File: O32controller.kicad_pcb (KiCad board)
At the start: 4 copper layers, 27 x 27 mm, 15 parts, among them J1 Conn_01x08_MountingPin, J2 Conn_01x02, J3 Motor Connection, J4 Motor Connection, J5 Motor Connection, J6 Motor Connection, Q1 CSD88584Q5DCT, Q2 CSD88584Q5DCT, Q3 CSD88584Q5DCT, U1 TMAG5170-Q1, U2 STSPIN32F0A

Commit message: more placement
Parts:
- added C1: 100nF, Capacitor_SMD:C_0402_1005Metric, F.Cu at (39.1, 55.6)
- added C10: 10nF, Capacitor_SMD:C_0402_1005Metric, F.Cu at (25.5, 28.4)
- added C2: 47uF, Capacitor_SMD:C_0603_1608Metric, F.Cu at (18.0, 28.7)
- added C3: 10uF, Capacitor_SMD:C_0603_1608Metric, F.Cu at (18.0, 31.2)
- added C4: 100nF, Capacitor_SMD:C_0402_1005Metric, F.Cu at (25.5, 30.4)
- added C5: 100nF, Capacitor_SMD:C_0402_1005Metric, F.Cu at (28.4, 28.4)
- added C6: 100nF, Capacitor_SMD:C_0402_1005Metric, F.Cu at (21.5, 30.9)
- added C7: 100nF, Capacitor_SMD:C_0402_1005Metric, F.Cu at (38.4, 22.3)
- added C8: 100uF, Capacitor_SMD:CP_Elec_6.3x7.7, F.Cu at (45.5, 40.4)
- added C9: 100uF, Capacitor_SMD:CP_Elec_6.3x7.7, F.Cu at (45.5, 59.4)
- added L1: 22uH, Inductor_SMD:L_0603_1608Metric, F.Cu at (22.0, 28.7)
- added R10: R_Small_US, Resistor_SMD:R_0402_1005Metric, F.Cu at (29.9, 37.1)
- added R11: R_Small_US, Resistor_SMD:R_0402_1005Metric, F.Cu at (32.8, 39.1)
- added R12: R_Small_US, Resistor_SMD:R_0402_1005Metric, F.Cu at (32.8, 37.1)
- added R13: 10R, Resistor_SMD:R_0402_1005Metric, F.Cu at (45.0, 24.3)
- added R14: 0R, Resistor_SMD:R_0402_1005Metric, F.Cu at (38.4, 20.3)
- added R15: 10R, Resistor_SMD:R_0402_1005Metric, F.Cu at (45.0, 22.3)
- added R16: 10R, Resistor_SMD:R_0402_1005Metric, F.Cu at (17.5, 41.0)
- added R18: 10R, Resistor_SMD:R_0402_1005Metric, F.Cu at (17.5, 39.1)
- added R19: 10R, Resistor_SMD:R_0402_1005Metric, F.Cu at (29.9, 41.0)
- added R2: R_Small_US, Resistor_SMD:R_0402_1005Metric, F.Cu at (45.0, 20.3)
- added R21: 10R, Resistor_SMD:R_0402_1005Metric, F.Cu at (29.9, 39.1)
- added R4: R_Small_US, Resistor_SMD:R_0402_1005Metric, F.Cu at (47.9, 20.3)
- added R6: R_Small_US, Resistor_SMD:R_0402_1005Metric, F.Cu at (17.5, 37.1)
- added R7: R_Small_US, Resistor_SMD:R_0402_1005Metric, F.Cu at (20.4, 39.1)
- added R8: R_Small_US, Resistor_SMD:R_0402_1005Metric, F.Cu at (20.4, 37.1)
- J2: value Conn_01x02 -> BATT+; footprint Connector_Wire:SolderWire-0.1sqmm_1x02_P3.6mm_D0.4mm_OD1mm -> Connector_Wire:SolderWire-0.1sqmm_1x01_D0.4mm_OD1mm
- J3: value Motor Connection -> BATT-
- J4, J5, J6: footprint Connector_Wire:SolderWire-0.1sqmm_1x01_D0.4mm_OD1mm -> Connector_Wire:SolderWire-0.75sqmm_1x01_D1.25mm_OD2.3mm
- R3: value 0.02R -> R_Small_US; footprint Resistor_SMD:R_0805_2012Metric -> Resistor_SMD:R_0402_1005Metric
- moved R3 27.6 mm to (34.0, 52.3)
- moved J6 13.7 mm to (61.7, 51.6)
- moved J5 12.2 mm to (61.7, 57.7)
- moved J2 11.1 mm to (57.1, 61.7)
- moved J3 8.18 mm to (54.1, 61.7)
- moved R9 6.86 mm to (61.8, 49.0), turned to 0 degrees
- moved R5 6.51 mm to (61.7, 55.1), turned to 0 degrees
- moved J4 6.17 mm to (61.7, 45.9)
- moved R1 2.17 mm to (61.8, 43.2)
- moved U2 1.72 mm to (45.6, 50.6)
- moved Q3 0.55 mm to (56.4, 50.0)
- moved U1 0.52 mm to (50.0, 50.0)
- moved Q2 0.49 mm to (56.4, 56.6)
- moved Q1 0.38 mm to (56.4, 43.4), turned to 90 degrees
- moved J1 0.07 mm to (50.0, 39.6)
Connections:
- net /Motor phase/Sense_P renamed /Motor phase U/Sense_N
- J1 pad 2: unconnected-(J1-Pad2) -> I2C_SCL
- J1 pad 3: unconnected-(J1-Pad3) -> I2C_SDA
- J1 pad 4: unconnected-(J1-Pad4) -> GND
- J1 pad 5: unconnected-(J1-Pad5) -> SWD_CLK
- J1 pad 6: unconnected-(J1-Pad6) -> SWD_IO
- J2 pad 1: unconnected-(J2-Pad1) -> VBUS
- J3 pad 1: /Motor phase/Motor -> GND
- R3 pad 2: GND -> /OP_U_N
- U2 pad 6: VBUS -> Net-(C3-Pad1)

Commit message: put everything on, need to choose caps
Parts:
- C10: moved to B.Cu
- J2, J3: footprint Connector_Wire:SolderWire-0.1sqmm_1x01_D0.4mm_OD1mm -> O32controller:SolderWire-Actual_1x01_D1.7mm_OD_2.5mm
- J4, J5, J6: footprint Connector_Wire:SolderWire-0.75sqmm_1x01_D1.25mm_OD2.3mm -> O32controller:SolderWire-Actual_1x01_D1.7mm_OD_2.5mm
- L1: footprint Inductor_SMD:L_0603_1608Metric -> Inductor_SMD:L_Wuerth_MAPI-3010
- moved C6 37.2 mm to (50.4, 54.4), turned to -90 degrees
- moved R18 37.1 mm to (52.2, 52.0)
- moved R4 35.4 mm to (45.2, 55.6), turned to 180 degrees
- moved R16 34.8 mm to (50.2, 52.8)
- moved R6 34.6 mm to (50.2, 48.2), turned to 180 degrees
- moved L1 32.3 mm to (39.0, 56.2)
- moved C2 31.0 mm to (37.8, 52.6), turned to 90 degrees
- moved C10 30.4 mm to (46.0, 50.8), turned to 90 degrees
- moved C5 30.3 mm to (49.8, 49.8), turned to -90 degrees
- moved R14 29.5 mm to (37.8, 49.8), turned to 90 degrees
- moved C4 28.9 mm to (48.6, 47.7), turned to -90 degrees
- moved R21 28.7 mm to (52.2, 57.2)
- moved R19 28.2 mm to (52.2, 58.4)
- moved R10 27.6 mm to (50.0, 56.0), turned to 180 degrees
- moved C3 25.9 mm to (37.8, 48.0)
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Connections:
- net Net-(C3-Pad1) renamed /VREG12
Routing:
- net /Motor phase U/GH_MOS: track 0.00 -> 5.35 mm, vias 0 -> 1
- net /OUTU: track 0.00 -> 5.33 mm, vias 0 -> 1
- net /Motor phase V/GH_MOS: track 0.00 -> 1.02 mm, vias 0 -> 1
- net /OUTV: track 0.00 -> 1.00 mm, vias 0 -> 1
- added copper zone on F.Cu, net /Motor phase U/Motor
- added copper zone on F.Cu, net /Motor phase V/Motor
- added copper zone on F.Cu, net /Motor phase W/Motor
- added copper zone on In1.Cu, net GND
- added copper zone on In2.Cu, net GND
- added copper zone on B.Cu, net VBUS
- added copper zone on F.Cu, net VBUS

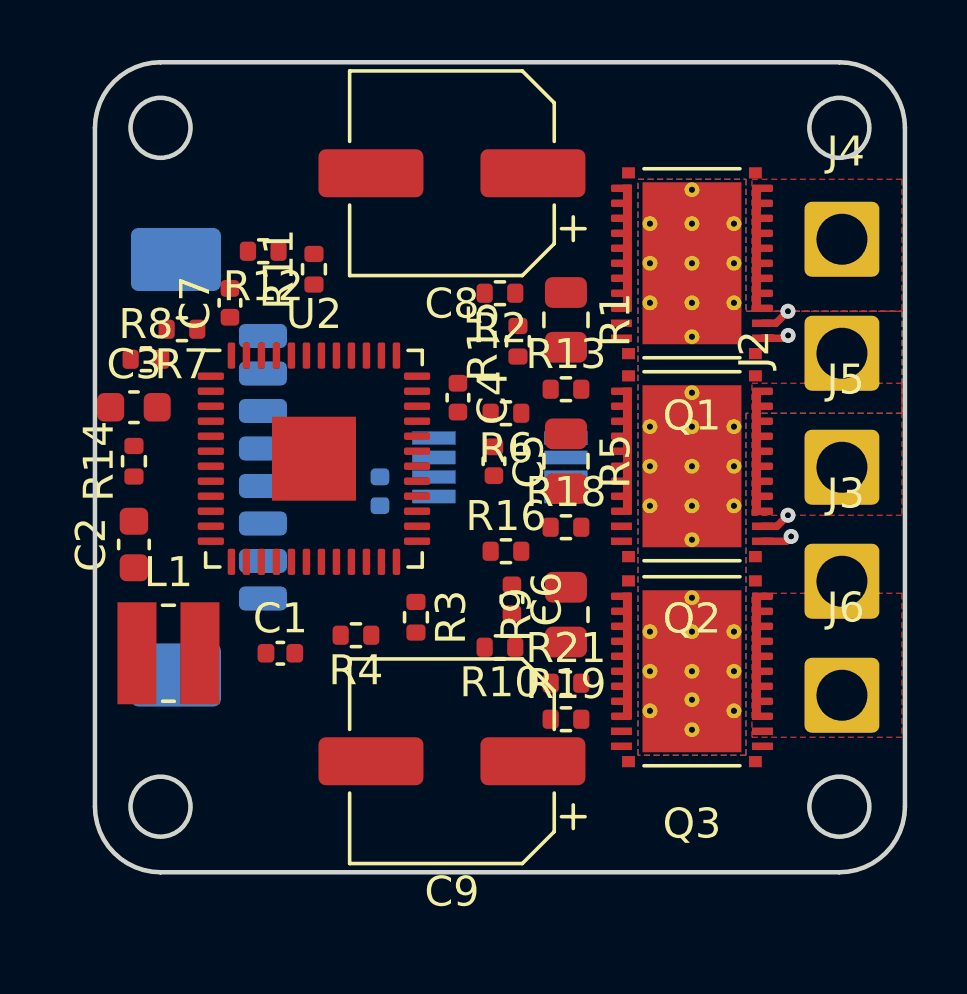
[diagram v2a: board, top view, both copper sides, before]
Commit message: fixed DRC, added as5047D, caps, ind
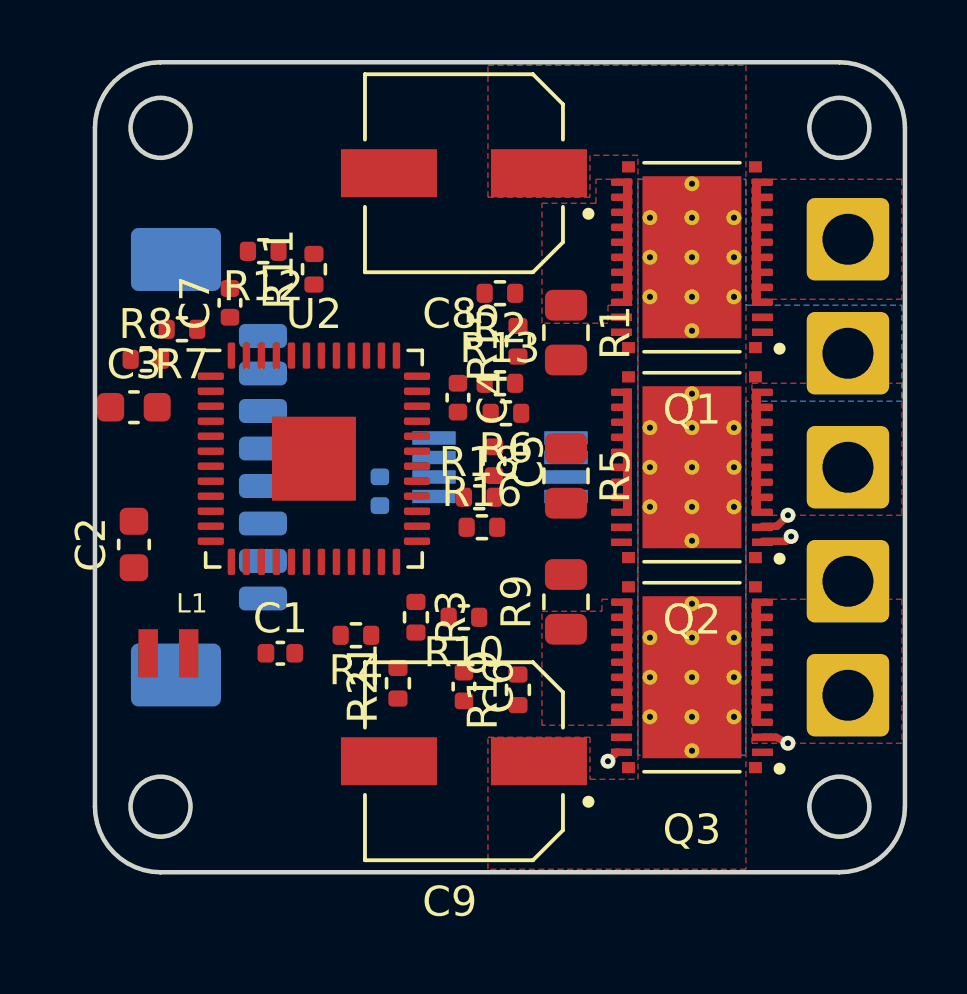
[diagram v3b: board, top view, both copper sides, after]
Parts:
- removed J2: BATT+, O32controller:SolderWire-Actual_1x01_D1.7mm_OD_2.5mm
- removed J3: BATT-, O32controller:SolderWire-Actual_1x01_D1.7mm_OD_2.5mm
- removed J4, J5, J6: Motor Connection, O32controller:SolderWire-Actual_1x01_D1.7mm_OD_2.5mm
- removed R14: 0R, Resistor_SMD:R_0402_1005Metric
- added GND: BATT-, O32controller:SolderWire-Actual_1x01_D1.7mm_OD_2.75mm, B.Cu at (61.6, 53.8)
- added U: Motor Connection, O32controller:SolderWire-Actual_1x01_D1.7mm_OD_2.75mm, B.Cu at (61.6, 42.4)
- added V: Motor Connection, O32controller:SolderWire-Actual_1x01_D1.7mm_OD_2.75mm, B.Cu at (61.6, 50.0)
- added Vin: BATT+, O32controller:SolderWire-Actual_1x01_D1.7mm_OD_2.75mm, B.Cu at (61.6, 46.2)
- added W: Motor Connection, O32controller:SolderWire-Actual_1x01_D1.7mm_OD_2.75mm, B.Cu at (61.6, 57.6)
- C8, C9: footprint Capacitor_SMD:CP_Elec_6.3x7.7 -> O32controller:CAP_EEEFN1E101UP
- L1: footprint Inductor_SMD:L_Wuerth_MAPI-3010 -> O32controller:IND_VLS201612CX-220M-1
- Q1, Q2, Q3: value CSD88584Q5DCT -> DMM0022A
- moved R21 5.60 mm to (46.6, 57.2), turned to 90 degrees
- moved C6 3.32 mm to (48.8, 57.3)
- moved R18 3.06 mm to (49.3, 51.0)
- moved R13 2.21 mm to (50.0, 47.2)
- moved R19 1.88 mm to (50.6, 57.4), turned to 90 degrees
- moved R10 1.56 mm to (48.8, 55.0)
- moved R16 1.13 mm to (49.4, 52.0)
- moved R5 0.49 mm to (52.2, 50.3)
- moved R1 0.43 mm to (52.2, 45.5)
- moved R9 0.43 mm to (52.2, 54.5)
- moved C8 0.40 mm to (48.8, 40.2)
- moved C9 0.40 mm to (48.8, 59.8)
- moved Q1 0.20 mm to (56.4, 43.0)
- moved Q3 0.20 mm to (56.4, 57.0)
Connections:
- C3 pad 1: /VREG12 -> VBUS
- U2 pad 6: /VREG12 -> VBUS
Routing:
- net /Motor phase U/GH_MOS: track 5.35 -> 4.10 mm, vias 1 -> 0
- net /OUTU: track 5.33 -> 4.31 mm, vias 1 -> 0
- net /OUTW: track 0.00 -> 0.90 mm, vias 0 -> 1
- net /Motor phase W/GL_MOS: track 0.00 -> 0.57 mm, vias 0 -> 1
- added copper zone on F.Cu, net /Motor phase U/Sense_P
- added copper zone on F.Cu, net /Motor phase W/Sense_P

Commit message: before big shunt:
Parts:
- removed GND: BATT-, O32controller:SolderWire-Actual_1x01_D1.7mm_OD_2.75mm
- removed U, V, W: Motor Connection, O32controller:SolderWire-Actual_1x01_D1.7mm_OD_2.75mm
- removed Vin: BATT+, O32controller:SolderWire-Actual_1x01_D1.7mm_OD_2.75mm
- added C11: 1nF, Capacitor_SMD:C_0402_1005Metric, F.Cu at (35.0, 50.2)
- added C12: 10nF, Capacitor_SMD:C_0402_1005Metric, F.Cu at (69.4, 52.8)
- added C13: 4.7nF, Capacitor_SMD:C_0402_1005Metric, F.Cu at (66.5, 54.8)
- added C14: 10nF, Capacitor_SMD:C_0402_1005Metric, F.Cu at (69.4, 45.3)
- added C15: 4.7nF, Capacitor_SMD:C_0402_1005Metric, F.Cu at (61.5, 52.0)
- added C16: 10nF, Capacitor_SMD:C_0402_1005Metric, F.Cu at (69.7, 48.6)
- added C17: 4.7nF, Capacitor_SMD:C_0402_1005Metric, F.Cu at (66.8, 50.6)
- added D1: SBA0540Q, Diode_SMD:D_DFN2L, F.Cu at (41.6, 40.6)
- added D2: ESDA17P20-1F2, Diode_SMD:D_0402_CSP, F.Cu at (41.8, 59.4)
- added J2: BATT+, O32controller:SolderWire-Actual_1x01_D1.7mm_OD_2.75mm, F.Cu at (61.6, 46.2)
- added J3: BATT-, O32controller:SolderWire-Actual_1x01_D1.7mm_OD_2.75mm, F.Cu at (61.6, 53.8)
- added J4: Motor Connection, O32controller:SolderWire-Actual_1x01_D1.7mm_OD_2.75mm, F.Cu at (61.6, 42.4)
- added J5: Motor Connection, O32controller:SolderWire-Actual_1x01_D1.7mm_OD_2.75mm, F.Cu at (61.6, 50.0)
- added J6: Motor Connection, O32controller:SolderWire-Actual_1x01_D1.7mm_OD_2.75mm, F.Cu at (61.6, 57.6)
- added R14: 2.2k, Resistor_SMD:R_0402_1005Metric, F.Cu at (29.2, 52.2)
- added R17: 2.2k, Resistor_SMD:R_0402_1005Metric, F.Cu at (32.1, 52.2)
- added R20: 2.2k, Resistor_SMD:R_0402_1005Metric, F.Cu at (32.1, 50.2)
- added R22: 121k, Resistor_SMD:R_0402_1005Metric, F.Cu at (29.2, 50.2)
- added R23: 2.21R, Resistor_SMD:R_0402_1005Metric, F.Cu at (66.5, 52.8)
- added R24: 2.21R, Resistor_SMD:R_0402_1005Metric, F.Cu at (66.5, 45.4)
- added R25: 2.21R, Resistor_SMD:R_0402_1005Metric, F.Cu at (66.8, 48.6)
- C10: value 10nF -> 100nF
- Q1, Q2, Q3: value DMM0022A -> CSD88584Q5DCT
- R1, R5, R9: value 0.02R -> WFCP06124L000FE66 0.004R; footprint Resistor_SMD:R_0805_2012Metric -> O32controller:RESC2550X76N
- R10, R11, R2, R3, R6, R7: value R_Small_US -> 1.78k
- R12, R4, R8: value R_Small_US -> 13.7k
- U1: value TMAG5170-Q1 -> AS5047D; footprint Package_SO:VSSOP-8_3.0x3.0mm_P0.65mm -> Package_SO:TSSOP-14_4.4x5mm_P0.65mm
- moved C4 6.60 mm to (42.0, 47.6)
- moved R13 6.60 mm to (43.4, 47.1)
- moved R16 6.60 mm to (42.8, 51.9)
- moved R18 6.60 mm to (42.7, 50.9)
- moved R19 6.60 mm to (44.0, 57.3)
- moved R3 6.60 mm to (40.6, 54.9)
- moved R6 6.60 mm to (43.6, 48.1)
- moved C5 6.60 mm to (43.2, 49.7)
- moved C6 6.60 mm to (42.2, 57.2)
- moved R10 6.60 mm to (42.2, 54.9)
- moved R15 2.40 mm to (48.2, 45.7)
- moved R2 2.21 mm to (47.8, 44.0)
- moved R5 1.04 mm to (51.2, 50.0)
- moved R1 1.00 mm to (51.2, 45.6)
- moved R9 1.00 mm to (51.2, 54.4)
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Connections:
- J1 pad 1: unconnected-(J1-Pad1) -> +3.3V
- J1 pad 4: GND -> /GPIO_PA15
- J1 pad 8: unconnected-(J1-Pad8) -> GND
- R1 pad 1: /Motor phase U/Sense_P -> GND
- R1 pad 2: GND -> /Motor phase U/Sense_P
- R5 pad 1: /Motor phase V/Sense_P -> GND
- R5 pad 2: GND -> /Motor phase V/Sense_P
- R9 pad 1: /Motor phase W/Sense_P -> GND
- R9 pad 2: GND -> /Motor phase W/Sense_P
- U1 pad 1: SPI_SCLK -> /~{MAG_CS}
- U1 pad 2: SPI_MOSI -> SPI_MISO
- U1 pad 3: SPI_MISO -> SPI_MOSI
- U1 pad 4: unconnected-(U1-Pad4) -> SPI_SCLK
- U1 pad 5: +3.3V -> unconnected-(U1-Pad5)
- U1 pad 6: GND -> unconnected-(U1-Pad6)
- U1 pad 7: GND -> unconnected-(U1-Pad7)
- U1 pad 8: ~{ALERT} -> unconnected-(U1-Pad8)
- U2 pad 15: unconnected-(U2-Pad15) -> /~{MAG_CS}
- U2 pad 19: unconnected-(U2-Pad19) -> /OP_U_O
- U2 pad 39: unconnected-(U2-Pad39) -> /GPIO_PA15
- U2 pad 4: /GPIO_PF0 -> /OP_V_O
- U2 pad 5: /GPIO_PF1 -> /OP_W_O

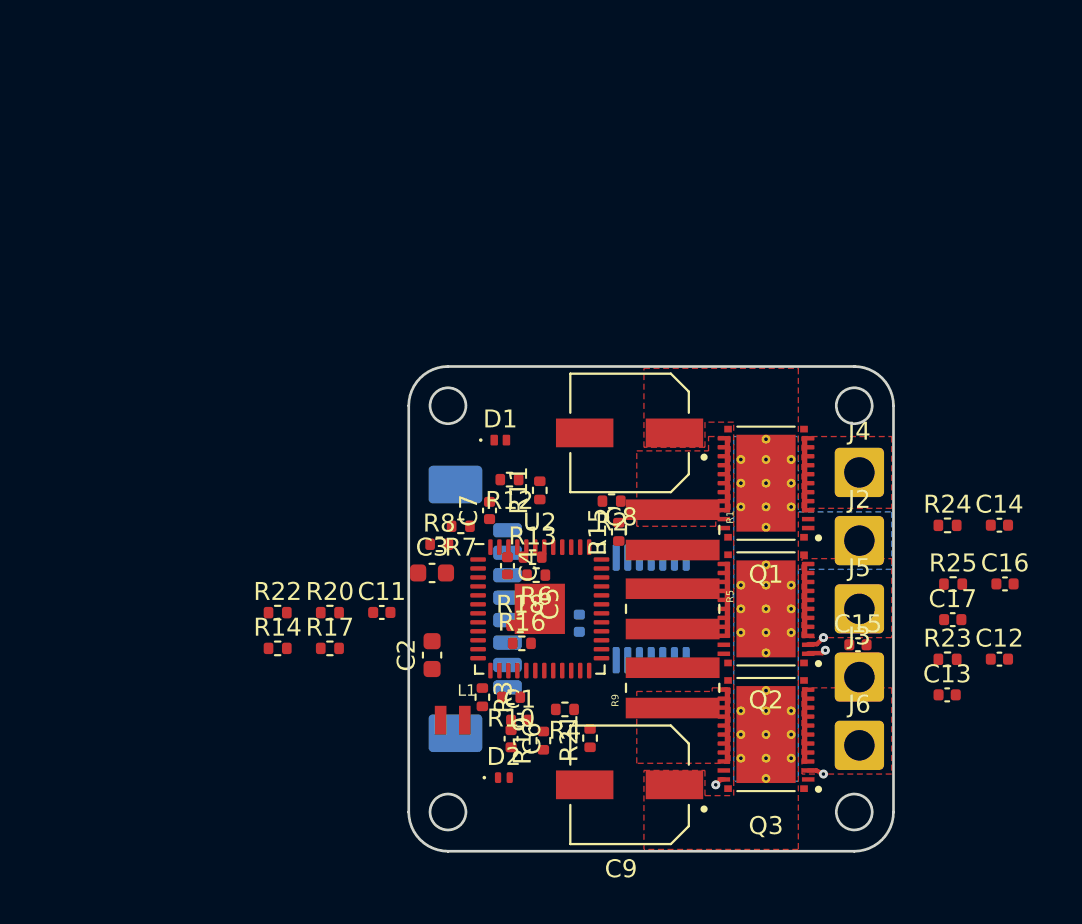
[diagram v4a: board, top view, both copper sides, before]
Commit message: used 2512 shunts to bridge vias
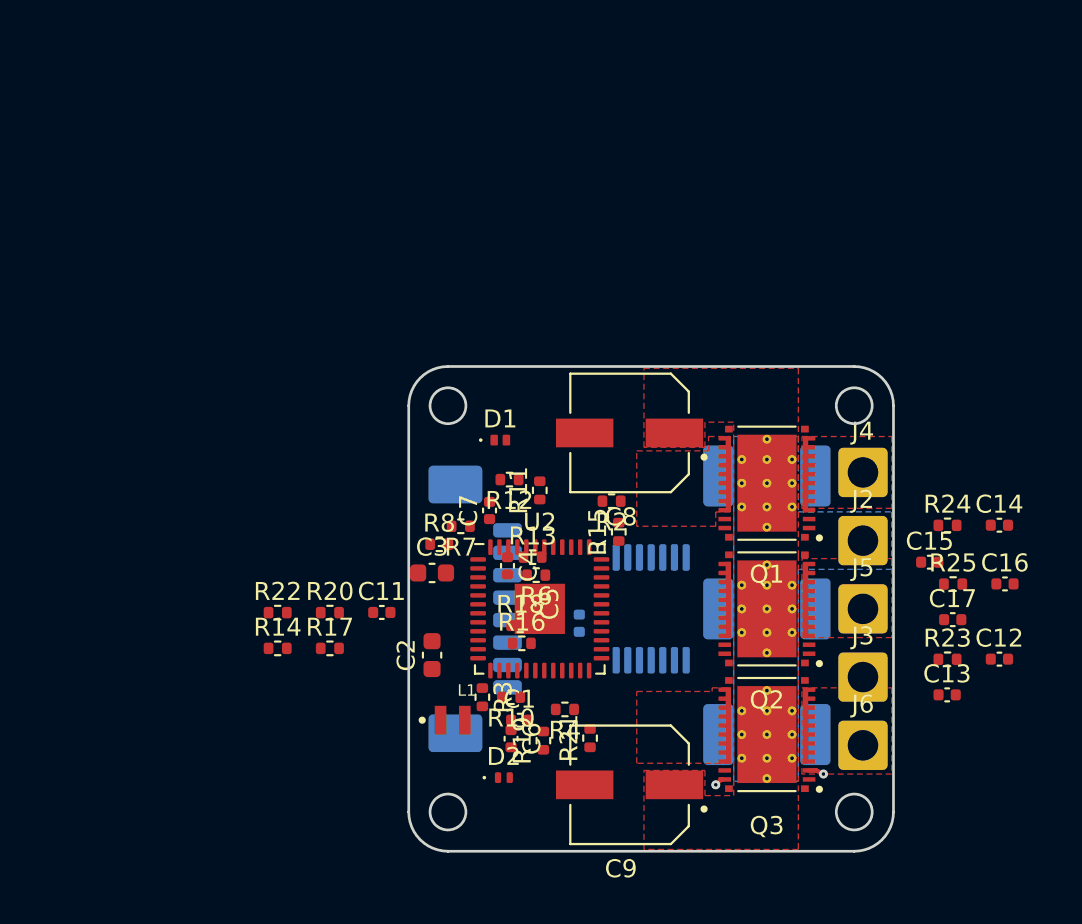
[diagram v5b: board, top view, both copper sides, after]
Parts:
- Q1, Q2, Q3: value CSD88584Q5DCT -> DMM0022A
- R1, R5, R9: footprint O32controller:RESC2550X76N -> Resistor_SMD:R_Shunt_2512_6332Metric; moved to B.Cu
- moved C15 6.10 mm to (65.5, 47.4)
- moved R1 6.05 mm to (56.5, 42.6), turned to 180 degrees
- moved R9 5.86 mm to (56.5, 57.0), turned to 180 degrees
- moved R5 5.25 mm to (56.5, 50.0), turned to 180 degrees
- moved J2 0.20 mm to (61.8, 46.2)
- moved J3 0.20 mm to (61.8, 53.8)
- moved J4 0.20 mm to (61.8, 42.4)
- moved J5 0.20 mm to (61.8, 50.0)
- moved J6 0.20 mm to (61.8, 57.6)
- moved Q1 0.05 mm to (56.5, 43.0)
- moved Q2 0.05 mm to (56.5, 50.0)
- moved Q3 0.05 mm to (56.5, 57.0)
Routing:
- net /Motor phase V/GH_MOS: track 1.02 -> 0.00 mm, vias 1 -> 0
- net /OUTV: track 1.00 -> 0.00 mm, vias 1 -> 0
